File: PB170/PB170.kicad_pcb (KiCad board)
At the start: 4 copper layers, 96.5 x 71.1 mm, 37 parts, among them J1 USB_C_Receptacle_USB2.0-Conne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, J2 USB_B_Micro, Q1 P-MOSFET-MLP_HS, Q2 BC817, SW1 SW_MEC_5E, SW2 SW_MEC_5E, U1 74HC00, U2 74HC08, U3 74HC4511D, U4 HEF4518BT

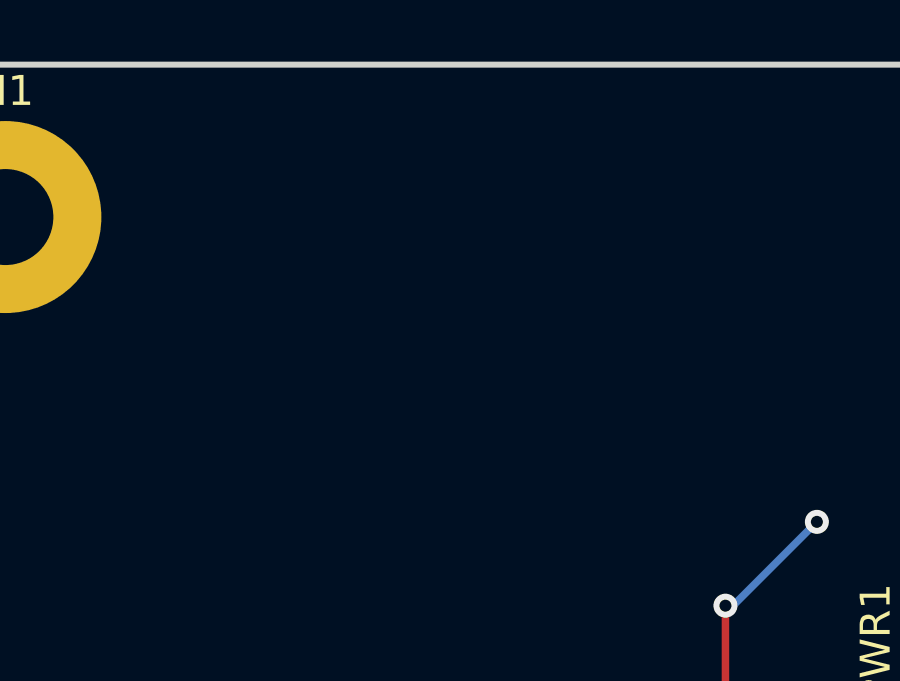
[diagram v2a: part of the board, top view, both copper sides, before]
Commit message: Added sample OR gate 74HC32.
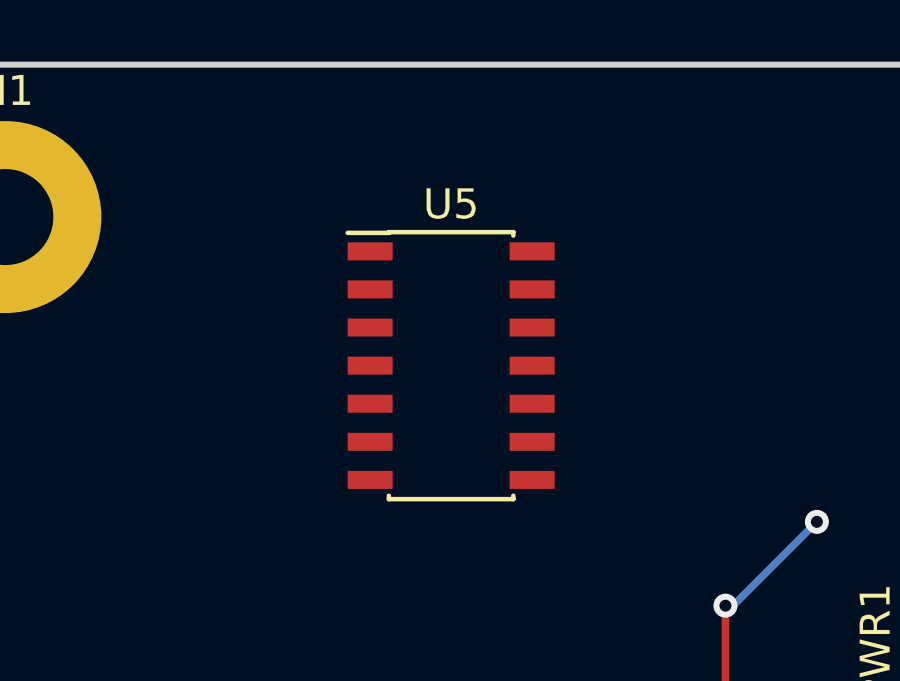
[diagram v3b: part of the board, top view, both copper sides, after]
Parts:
- added U5: 74HC32, Housings_SOIC:SOIC-14_3.9x8.7mm_Pitch1.27mm, F.Cu at (60.6, 35.4)

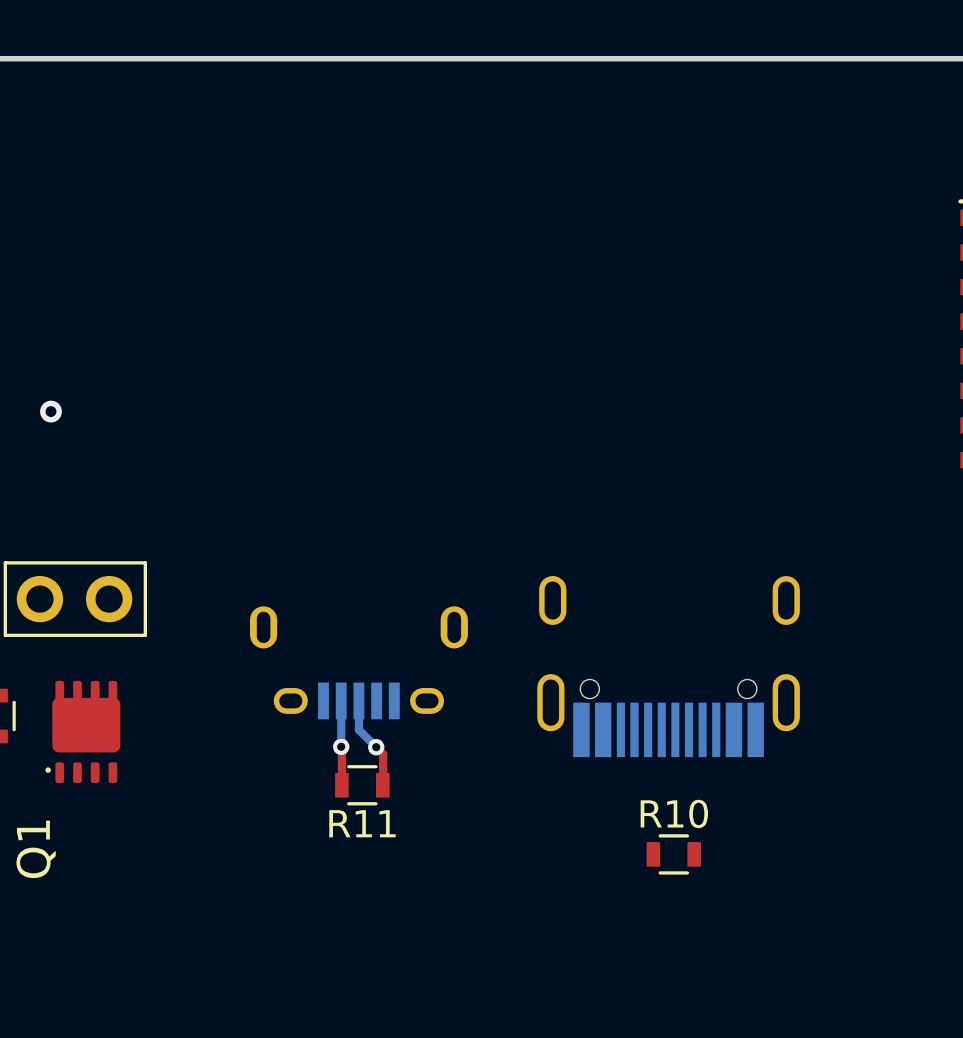
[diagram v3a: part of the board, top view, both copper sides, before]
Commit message: Created examples with new THT parts.
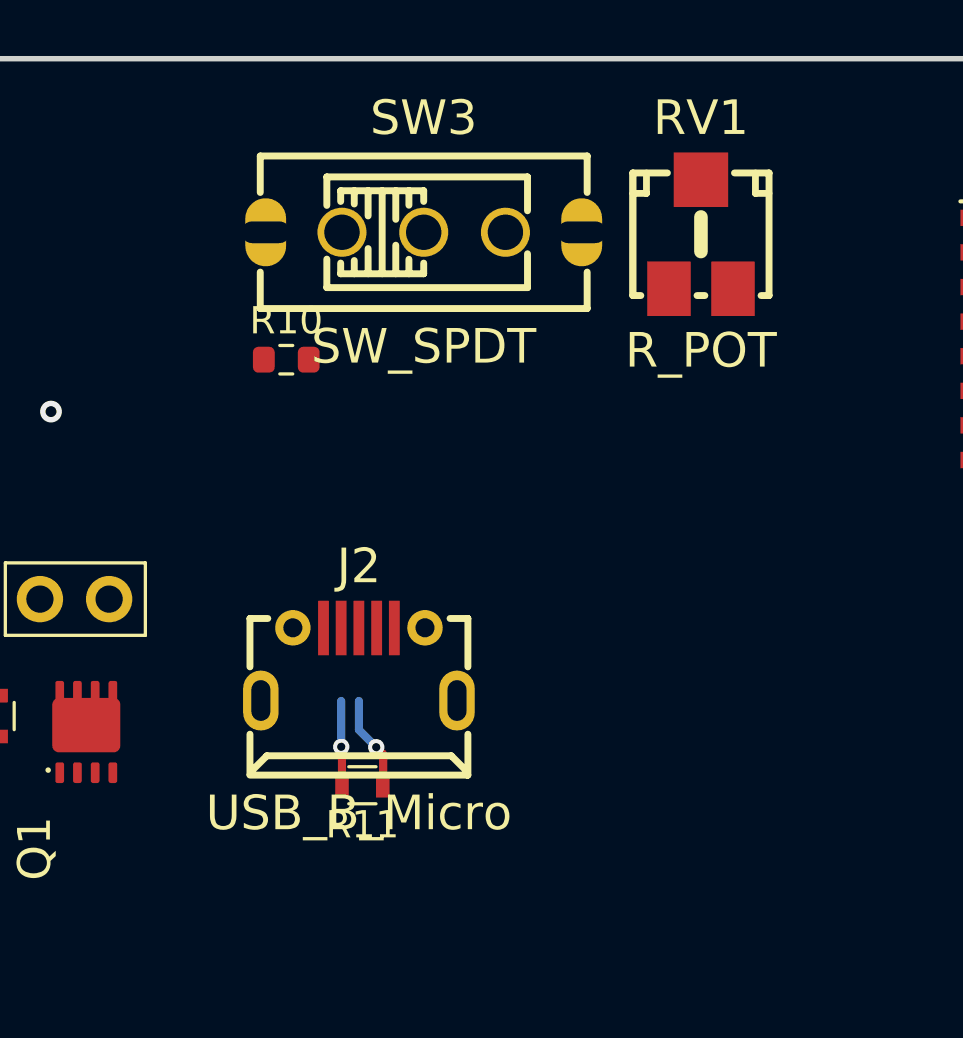
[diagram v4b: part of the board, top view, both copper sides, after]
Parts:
- removed J1: USB_C_Receptacle_USB2.0-Connector, PB170:USB_C_Female-16Pin-HPJF
- added RV1: R_POT, PB170:potentiometer10k, F.Cu at (103.9, 31.8)
- added SW3: SW_SPDT, PB170:toggleSwitch, F.Cu at (93.7, 31.8)
- J2: footprint Connectors:USB_Micro-B -> PB170:MICRO-USB-SMD_MICROXNJ; moved to F.Cu
- R10: value 220R -> 10k; footprint Resistors_SMD:R_0603 -> Resistor_SMD:R_0603_1608Metric
- moved R10 23.1 mm to (88.6, 36.4)
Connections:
- R10 pad 2: Net-(J1-PadA7) -> GND
